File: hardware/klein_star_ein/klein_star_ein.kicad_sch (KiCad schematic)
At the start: 195 parts, among them J1 USB_A, J10 AudioJack3_Ground_Switch, J11 AudioJack3_Ground_Switch, J12 AudioJack3_Ground_Switch, J2 DB15_Female_HighDensity_Mount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, J3 Bus_PCI_Express_x1, J4 1367073-1, J5 ARJM11C7-502-AB-ER2-T, J6 USB_C_Receptacle, J7 MEM2051-00-195-00-A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

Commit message: Prototype of power section footprint
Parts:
- C91: footprint Capacitor_SMD:C_0402_1005Metric -> Capacitor_SMD:C_0603_1608Metric
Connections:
- net 1.35_DRAM is gone; now on net 1V35_DRAM_VCORE: C76.1, L7.2, R16.1, TP7.1, U18.6 (OUT)
- net TX0: now reaches U11.24 (TXD0)
- net TX1: now reaches U11.25 (TXD1)
- net TX2: now reaches U11.26 (TXD2)
- net TX3: now reaches U11.27 (TXD3)
- net TX_CLK: now reaches U11.32 (GTX_CLK)
- net TX_CTRL: now reaches U11.33 (TX_EN)
- net RX3: now reaches U11.36 (RXD3/MODE3)
- net RX2: now reaches U11.38 (RXD2/MODE2)
- net RX1: now reaches U11.41 (RXD1/MODE1)
- net RX0: now reaches U11.42 (RXD0/MODE0)
- net RX_CTRL: now reaches U11.43 (RX_DV/CLK125_EN)
- net RX_CLK: now reaches U11.46 (RX_CLK/PHYAD2)
- net MDC: now reaches U11.48 (MDC)
- net MDIO: now reaches U11.49 (MDIO)
- net INT: now reaches U11.51 (INT_N)
- net CLK125: now reaches U11.55 (CLK125_NDO/LED_MODE)
- net RESET: now reaches U11.56 (nRESET)
- net 1.2_FPGA renamed 1V2_FPGA
- no-connect marks 78 -> 79
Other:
- note added: "TODO: ISET and XO XI pins"
- note added: "TODO: TRCT pins"

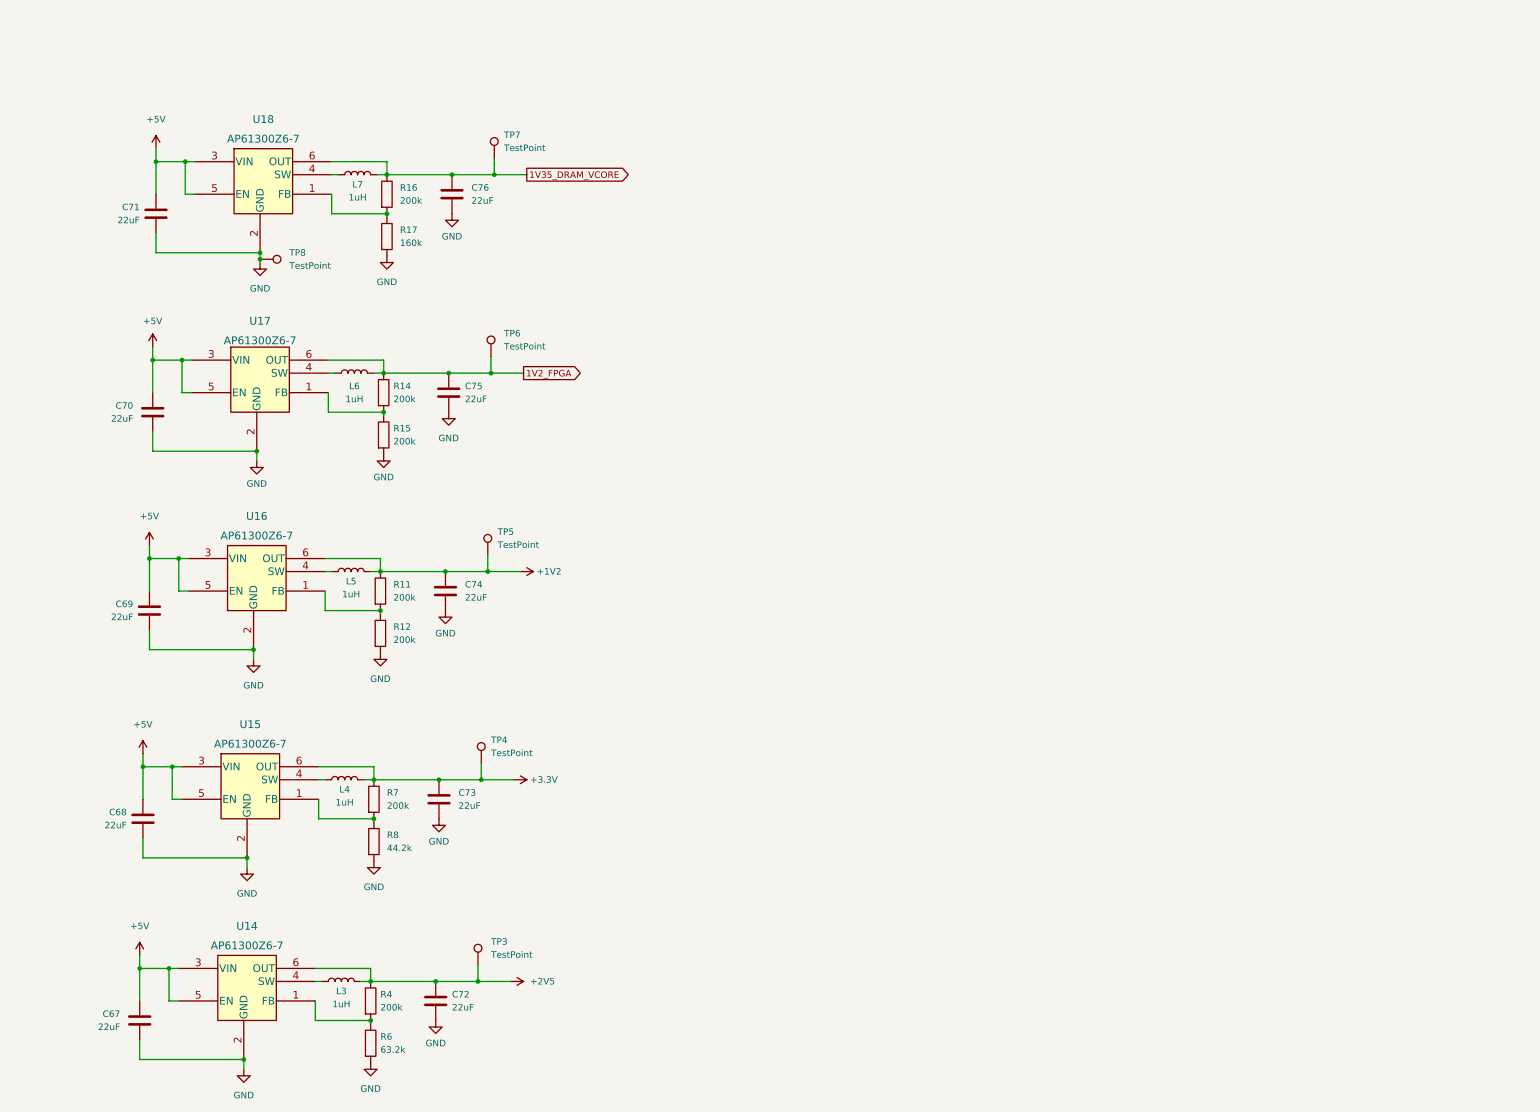
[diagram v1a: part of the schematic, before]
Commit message: Implmented power sections as hierarchical sheet
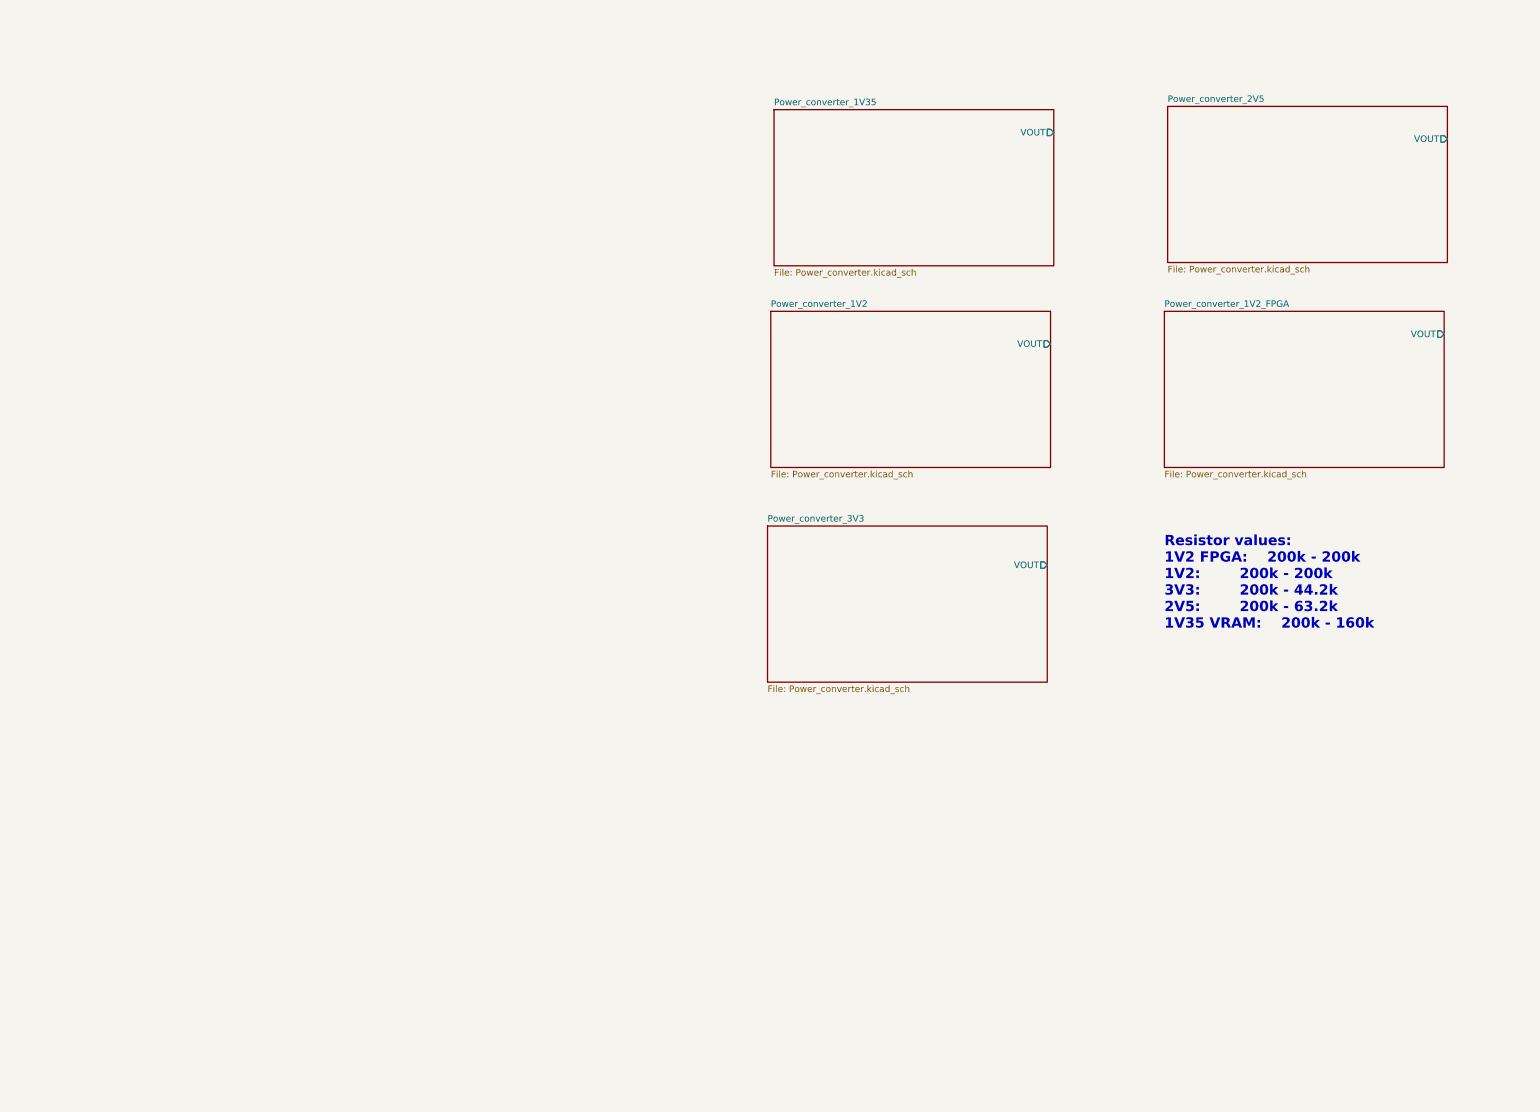
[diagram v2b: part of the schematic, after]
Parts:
- removed C67, C68, C69, C70, C71, C72, C73, C74, C75, C76: 22uF, Capacitor_SMD:C_0402_1005Metric, symbol Device:C
- removed L3, L4, L5, L6, L7: 1uH, Inductor_SMD:L_0603_1608Metric, symbol Device:L
- removed R11, R12, R14, R15, R16, R4, R7: 200k, Resistor_SMD:R_0402_1005Metric_Pad0.72x0.64mm_HandSolder, symbol Device:R
- removed R17: 160k, Resistor_SMD:R_0402_1005Metric_Pad0.72x0.64mm_HandSolder, symbol Device:R
- removed R6: 63.2k, Resistor_SMD:R_0402_1005Metric_Pad0.72x0.64mm_HandSolder, symbol Device:R
- removed R8: 44.2k, Resistor_SMD:R_0402_1005Metric_Pad0.72x0.64mm_HandSolder, symbol Device:R
- removed TP3, TP4, TP5, TP6, TP7: TestPoint, TestPoint:TestPoint_Pad_1.0x1.0mm, symbol Connector:TestPoint
- removed TP8: TestPoint, TestPoint:TestPoint_Loop_D1.80mm_Drill1.0mm_Beaded, symbol Connector:TestPoint
- removed U14, U15, U16, U17, U18: AP61300Z6-7, Package_TO_SOT_SMD:SOT-563, symbol AP61300Z6-7:AP61300Z6-7
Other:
- added sheet Power_converter_1V2 (Power_converter.kicad_sch)
- added sheet Power_converter_1V2_FPGA (Power_converter.kicad_sch)
- added sheet Power_converter_1V35 (Power_converter.kicad_sch)
- added sheet Power_converter_2V5 (Power_converter.kicad_sch)
- added sheet Power_converter_3V3 (Power_converter.kicad_sch)
- note added: "Resistor values: 1V2 FPGA: 200k - 200k 1V2: 200k - 200k 3V3: 200k - 44.2k 2V5: 200k - 63.2k 1V35 VRAM: 200k - 160k"
